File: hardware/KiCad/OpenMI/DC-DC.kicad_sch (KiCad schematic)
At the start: 13 parts

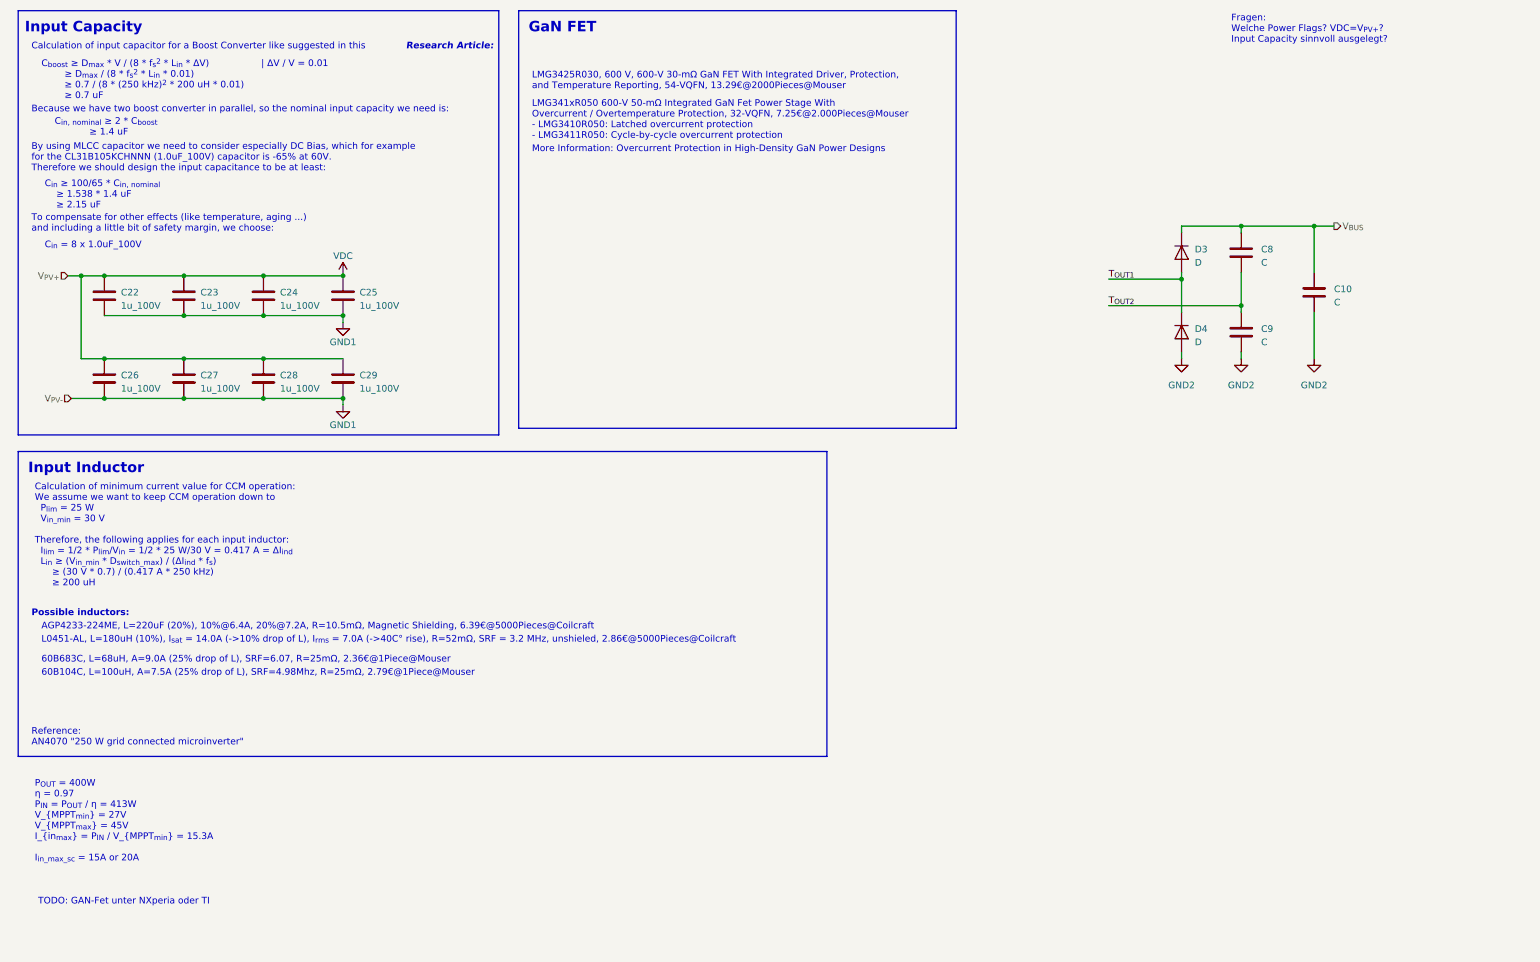
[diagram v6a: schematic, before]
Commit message: feat(hw): add input inductance and calculations for it
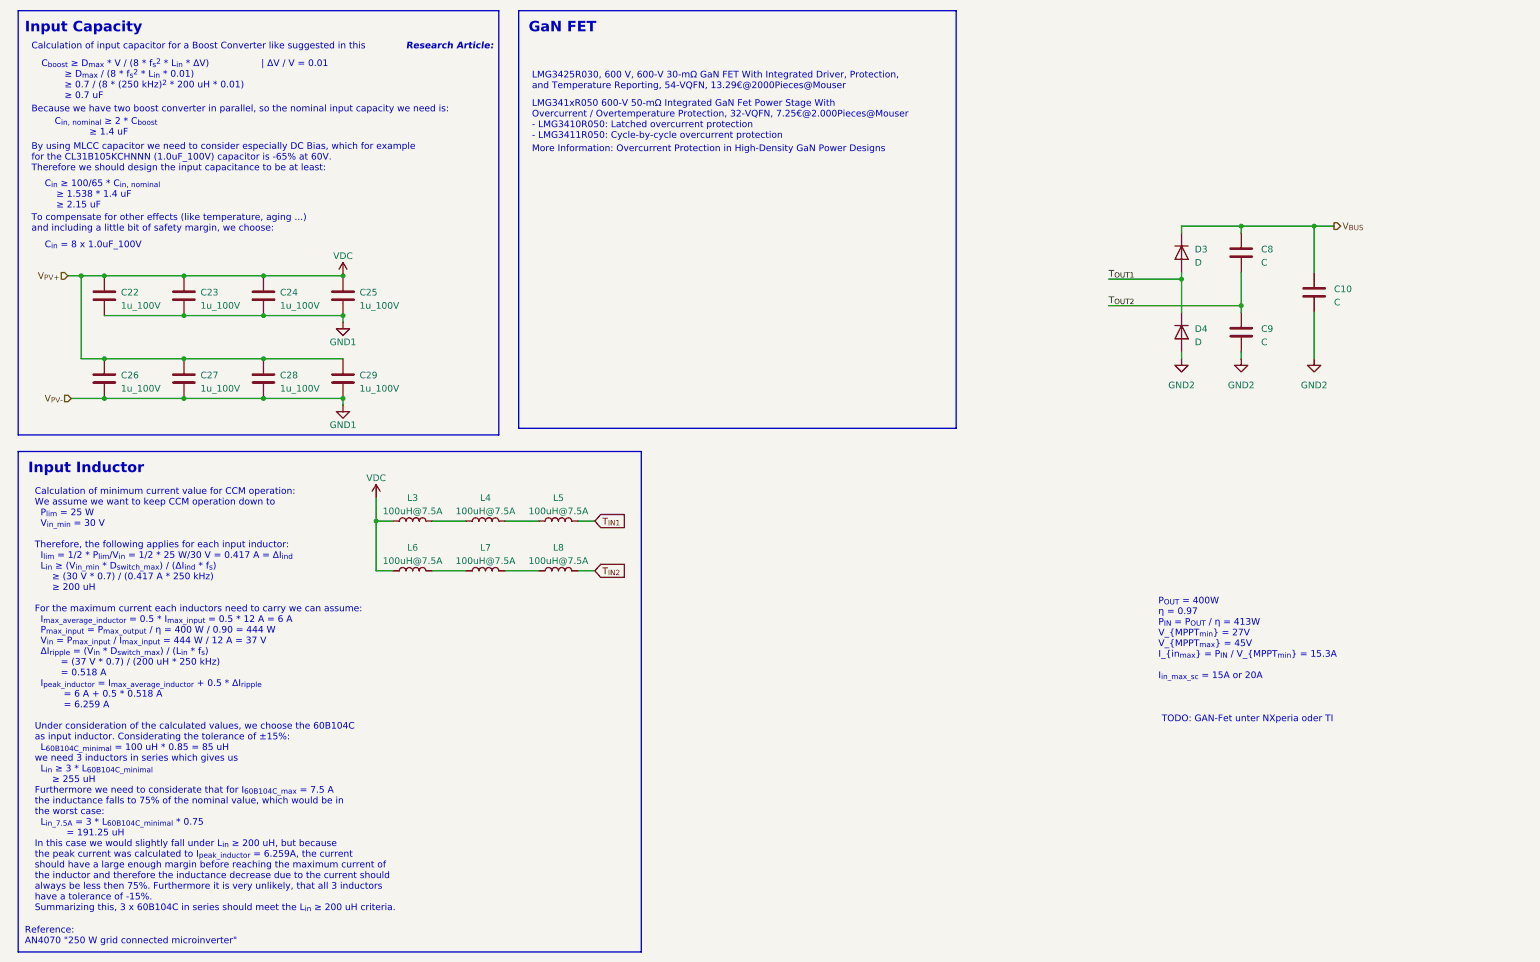
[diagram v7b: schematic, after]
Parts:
- added L3, L4, L5, L6, L7, L8: 100uH@7.5A, OpenCE:L_6000B_Series_Murata, symbol _L_Power:100uH@7.5A
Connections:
- net VDC: now also L3.1, L6.1
- new net: L6.2, L7.1
- new net: L7.2, L8.1
- new net: L4.2, L5.1
- new net: L3.2, L4.1
- new net T_{IN1}: L5.2
- new net T_{IN2}: L8.2
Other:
- note added: "Calculation of minimum current value for CCM operation: We assume we want to keep CCM operation down to P_{lim} = 25 W V_{in_min} = 30 V Therefore, the following applies for each input inductor: I_{lim} = 1/2 * P_{lim}/V_{in} = 1/2 * 25 W/30 V = 0.417 A = ΔI_{ind} L_{in} ≥ (V_{in_min} * D_{switch_max}) / (ΔI_{ind} * f_{s}) ≥ (30 V * 0.7) / (0.417 A * 250 kHz) ≥ 200 uH For the maximum current each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"
- note removed: "60B104C, L=100uH, A=7.5A (25% drop of L), SRF=4.98Mhz, R=25mΩ, 2.79€@1Piece@Mouser"
- note removed: "60B683C, L=68uH, A=9.0A (25% drop of L), SRF=6.07, R=25mΩ, 2.36€@1Piece@Mouser"
- note removed: "AGP4233-224ME, L=220uF (20%), 10%@6.4A, 20%@7.2A, R=10.5mΩ, Magnetic Shielding, 6.39€@5000Pieces@Coilcraft"
- note removed: "Calculation of minimum current value for CCM operation: We assume we want to keep CCM operation down to P_{lim} = 25 W V_{in_min} = 30 V Therefore, the following applies for each input inductor: I_{lim} = 1/2 * P_{lim}/V_{in} = 1/2 * 25 W/30 V = 0.417 A = ΔI_{ind} L_{in} ≥ (V_{in_min} * D_{switch_max}) / (ΔI_{ind} * f_{s}) ≥ (30 V * 0.7) / (0.417 A * 250 kHz) ≥ 200 uH"
- note removed: "Fragen: Welche Power Flags? VDC=V_{PV+}? Input Capacity sinnvoll ausgelegt?"
- note removed: "L0451-AL, L=180uH (10%), I_{sat} = 14.0A (->10% drop of L), I_{rms} = 7.0A (->40C° rise), R=52mΩ, SRF = 3.2 MHz, unshieled, 2.86€@5000Pieces@Coilcraft"
- note removed: "Possible inductors:"

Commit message: feat(hw): add GaN FET GAN7R0-150LBEZ and first considerations for gate driver
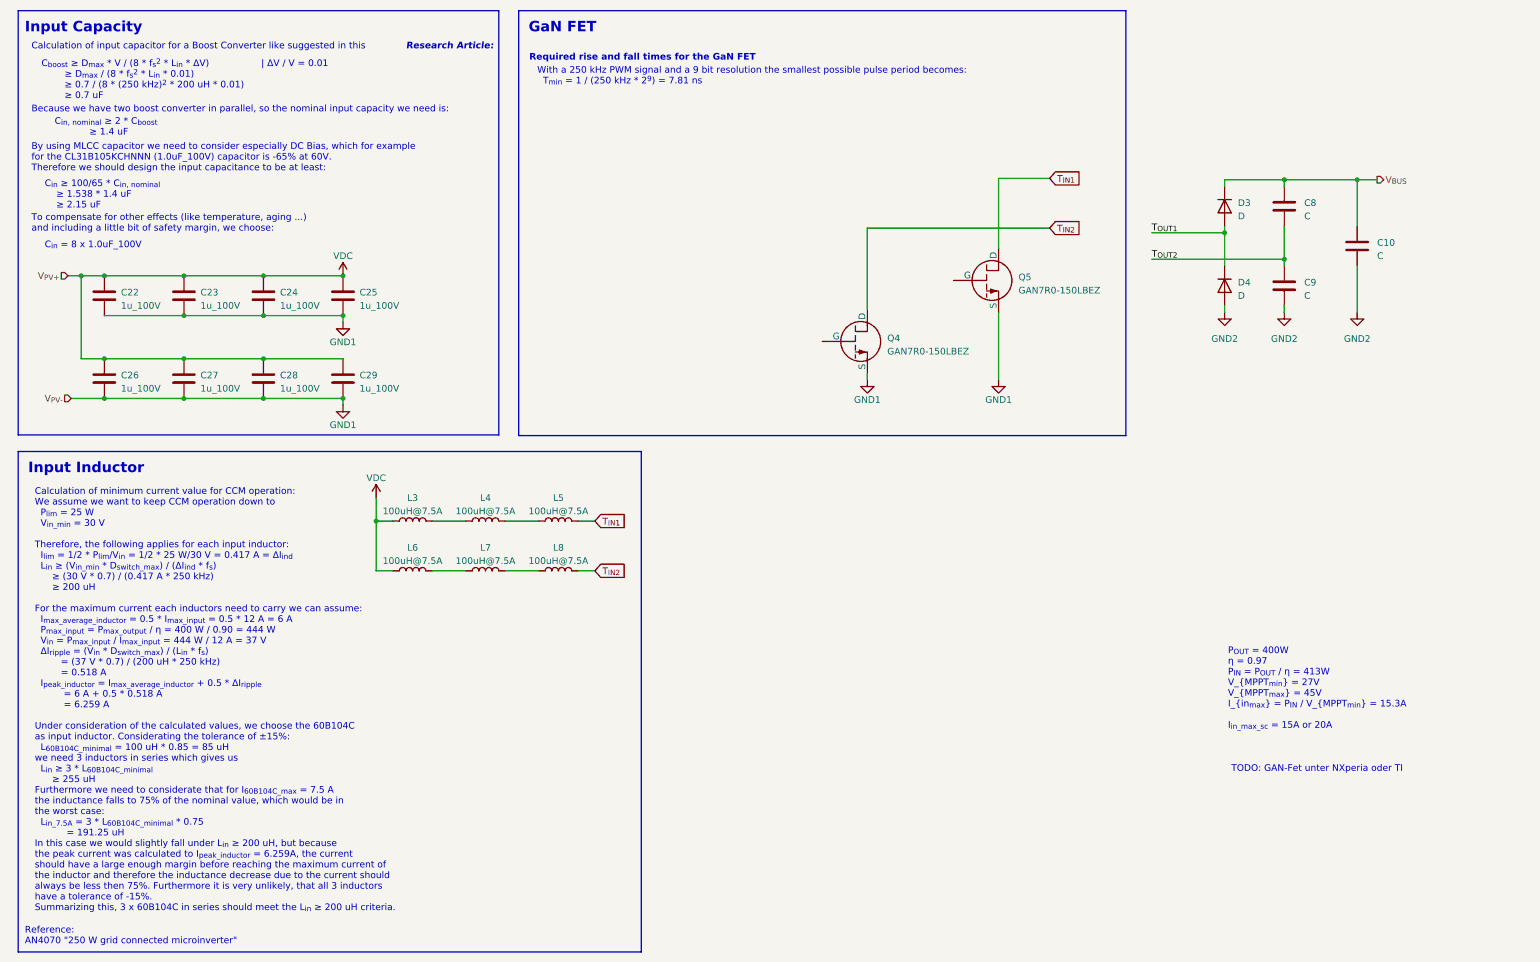
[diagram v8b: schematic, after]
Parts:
- added Q4, Q5: GAN7R0-150LBEZ, OpenCE:SOT8073-1, symbol _Transistor_FET:GAN7R0-150LBEZ
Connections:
- net GND1: now also Q4.3 (S), Q5.3 (S)
- net T_{IN1}: now also Q5.1 (D)
- net T_{IN2}: now also Q4.1 (D)
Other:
- note added: "Required rise and fall times for the GaN FET"
- note added: "With a 250 kHz PWM signal and a 9 bit resolution the smallest possible pulse period becomes: T_{min} = 1 / (250 kHz * 2^{9}) = 7.81 ns"
- note removed: "LMG341xR050 600-V 50-mΩ Integrated GaN Fet Power Stage With Overcurrent / Overtemperature Protection, 32-VQFN, 7.25€@2.000Pieces@Mouser - LMG3410R050: Latched overcurrent protection - LMG3411R050: Cycle-by-cycle overcurrent protection"
- note removed: "LMG3425R030, 600 V, 600-V 30-mΩ GaN FET With Integrated Driver, Protection, and Temperature Reporting, 54-VQFN, 13.29€@2000Pieces@Mouser"
- note removed: "More Information: Overcurrent Protection in High-Density GaN Power Designs"
- moved on the sheet: C10, C8, C9, D3, D4
